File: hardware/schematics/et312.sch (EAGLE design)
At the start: 119 parts, among them IC1 LM324N, IC2 4066N, IC3 LM358, IC4 7809, IC5 LM358N, IC6 7809, J1 BATTERY_CONNDEANS, Q1 IRL520N-H, Q2 IRL520N-H, Q3 IRF9Z24, Q4 IRL520N-H, Q5 IRL520N-H, Q6 IRF9Z24, Q7 2N3906, T1 2N3904, U1 MEGA16-P, U9 7805, X1 HD44780LCD-1602, X2 STEREOJACK, X3 STEREOJACK, X4 STEREOJACK, X5 STEREOJACK, X6 STEREOJACK

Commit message: Schematics
WIP
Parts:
- removed T2, T3: (no value), Eagle_POWER_MAGNETICS_rev16b:WE-FB_LT35XX/LT3748_EFD25_750310988
- added TR1, TR2: 42TL025, trafo-xicon:42TL025
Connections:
- removed net N$66: T3.3, X6.1
- removed net N$67: T3.2, X6.2, X6.5
- removed net N$77: T2.3, X5.1
- removed net N$78: T2.2, X5.2, X5.5
- new net N$16: TR1.6, X5.2, X5.5
- new net N$49: TR2.6, X6.2, X6.5
- new net N$50: TR2.4, X6.1
- new net N$6: TR1.4, X5.1
- net N$34: now also TR1.1; no longer T2.1
- net N$35: now also TR1.2; no longer T2.5
- net N$36: now also TR2.1; no longer T3.1
- net N$37: now also TR2.2; no longer T3.5
- net N$38: now also TR2.3; no longer T3.4
- net N$39: now also TR1.3; no longer T2.4
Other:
- note removed: "Possible transformer: Wurth 750811048"
- moved on the sheet: X5, X6
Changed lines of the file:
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@@
 <part name="R52" library="eagle-ltspice" deviceset="R" device="0207/10" value="0.5R"/>
 <part name="GND21" library="supply1" deviceset="GND" device=""/>
-<part name="T2" library="Eagle_POWER_MAGNETICS_rev16b" deviceset="WE-FB_LT35XX/LT3748_EFD25_750310988" device=""/>
-<part name="T3" library="Eagle_POWER_MAGNETICS_rev16b" deviceset="WE-FB_LT35XX/LT3748_EFD25_750310988" device=""/>
+<part name="TR1" library="trafo-xicon" deviceset="42T?*" device="L" technology="025"/>
+<part name="TR2" library="trafo-xicon" deviceset="42T?*" device="L" technology="025"/>
 </parts>
 <sheets>
@@
 <plain>
 <text x="99.06" y="7.62" size="1.778" layer="91">Output Stage</text>
-<text x="157.48" y="119.38" size="1.27" layer="97">Possible transformer: Wurth 750811048</text>
 </plain>
 <instances>
@@
 <instance part="+9V5" gate="G$1" x="60.96" y="142.24"/>
 <instance part="+9V6" gate="G$1" x="109.22" y="111.76"/>
-<instance part="X5" gate="1" x="187.96" y="134.62"/>
-<instance part="X6" gate="1" x="187.96" y="53.34"/>
+<instance part="X5" gate="1" x="195.58" y="134.62"/>
+<instance part="X6" gate="1" x="195.58" y="53.34"/>
 <instance part="R52" gate="G$1" x="40.64" y="154.94" rot="R90"/>
 <instance part="GND21" gate="1" x="40.64" y="144.78"/>
-<instance part="T2" gate="G$1" x="162.56" y="132.08"/>
-<instance part="T3" gate="G$1" x="162.56" y="50.8"/>
+<instance part="TR1" gate="G$1" x="167.64" y="132.08"/>
+<instance part="TR2" gate="G$1" x="167.64" y="50.8"/>
 </instances>
 <busses>
@@
 <wire x1="121.92" y1="157.48" x2="152.4" y2="157.48" width="0.1524" layer="91"/>
 <wire x1="152.4" y1="157.48" x2="152.4" y2="137.16" width="0.1524" layer="91"/>
-<wire x1="157.48" y1="137.16" x2="152.4" y2="137.16" width="0.1524" layer="91"/>
-<pinref part="T2" gate="G$1" pin="1"/>
+<wire x1="160.02" y1="137.16" x2="152.4" y2="137.16" width="0.1524" layer="91"/>
+<pinref part="TR1" gate="G$1" pin="1"/>
 </segment>
 </net>
@@
 <segment>
 <pinref part="Q3" gate="G$1" pin="D"/>
-<wire x1="124.46" y1="132.08" x2="157.48" y2="132.08" width="0.1524" layer="91"/>
-<pinref part="T2" gate="G$1" pin="5"/>
+<wire x1="124.46" y1="132.08" x2="160.02" y2="132.08" width="0.1524" layer="91"/>
+<pinref part="TR1" gate="G$1" pin="2"/>
 </segment>
 </net>
@@
 <wire x1="121.92" y1="81.28" x2="152.4" y2="81.28" width="0.1524" layer="91"/>
 <wire x1="152.4" y1="81.28" x2="152.4" y2="55.88" width="0.1524" layer="91"/>
-<wire x1="157.48" y1="55.88" x2="152.4" y2="55.88" width="0.1524" layer="91"/>
-<pinref part="T3" gate="G$1" pin="1"/>
+<wire x1="160.02" y1="55.88" x2="152.4" y2="55.88" width="0.1524" layer="91"/>
+<pinref part="TR2" gate="G$1" pin="1"/>
 </segment>
 </net>
@@
 <segment>
 <pinref part="Q6" gate="G$1" pin="D"/>
-<wire x1="124.46" y1="50.8" x2="157.48" y2="50.8" width="0.1524" layer="91"/>
-<pinref part="T3" gate="G$1" pin="5"/>
+<wire x1="124.46" y1="50.8" x2="160.02" y2="50.8" width="0.1524" layer="91"/>
+<pinref part="TR2" gate="G$1" pin="2"/>
 </segment>
 </net>
@@
 <wire x1="124.46" y1="22.86" x2="152.4" y2="22.86" width="0.1524" layer="91"/>
 <wire x1="152.4" y1="22.86" x2="152.4" y2="45.72" width="0.1524" layer="91"/>
-<wire x1="157.48" y1="45.72" x2="152.4" y2="45.72" width="0.1524" layer="91"/>
-<pinref part="T3" gate="G$1" pin="4"/>
+<wire x1="160.02" y1="45.72" x2="152.4" y2="45.72" width="0.1524" layer="91"/>
+<pinref part="TR2" gate="G$1" pin="3"/>
 </segment>
 </net>
@@
 <wire x1="124.46" y1="104.14" x2="152.4" y2="104.14" width="0.1524" layer="91"/>
 <wire x1="152.4" y1="104.14" x2="152.4" y2="127" width="0.1524" layer="91"/>
-<wire x1="157.48" y1="127" x2="152.4" y2="127" width="0.1524" layer="91"/>
-<pinref part="T2" gate="G$1" pin="4"/>
+<wire x1="160.02" y1="127" x2="152.4" y2="127" width="0.1524" layer="91"/>
+<pinref part="TR1" gate="G$1" pin="3"/>
 </segment>
 </net>
@@
 </segment>
 </net>
-<net name="N$66" class="0">
-<segment>
-<pinref part="X6" gate="1" pin="1"/>
-<wire x1="175.26" y1="45.72" x2="170.18" y2="45.72" width="0.1524" layer="91"/>
-<wire x1="170.18" y1="45.72" x2="170.18" y2="48.26" width="0.1524" layer="91"/>
-<wire x1="170.18" y1="48.26" x2="167.64" y2="48.26" width="0.1524" layer="91"/>
-<pinref part="T3" gate="G$1" pin="3"/>
-</segment>
-</net>
-<net name="N$67" class="0">
-<segment>
-<pinref part="X6" gate="1" pin="5"/>
-<wire x1="175.26" y1="55.88" x2="172.72" y2="55.88" width="0.1524" layer="91"/>
-<pinref part="X6" gate="1" pin="2"/>
-<wire x1="172.72" y1="55.88" x2="172.72" y2="53.34" width="0.1524" layer="91"/>
-<wire x1="172.72" y1="53.34" x2="172.72" y2="48.26" width="0.1524" layer="91"/>
-<wire x1="172.72" y1="48.26" x2="175.26" y2="48.26" width="0.1524" layer="91"/>
-<pinref part="T3" gate="G$1" pin="2"/>
-<wire x1="167.64" y1="53.34" x2="172.72" y2="53.34" width="0.1524" layer="91"/>
-<junction x="172.72" y="53.34"/>
-</segment>
-</net>
-<net name="N$77" class="0">
-<segment>
-<pinref part="X5" gate="1" pin="1"/>
-<wire x1="175.26" y1="127" x2="170.18" y2="127" width="0.1524" layer="91"/>
-<wire x1="170.18" y1="127" x2="170.18" y2="129.54" width="0.1524" layer="91"/>
-<wire x1="170.18" y1="129.54" x2="167.64" y2="129.54" width="0.1524" layer="91"/>
-<pinref part="T2" gate="G$1" pin="3"/>
-</segment>
-</net>
-<net name="N$78" class="0">
-<segment>
-<pinref part="X5" gate="1" pin="5"/>
-<wire x1="175.26" y1="137.16" x2="172.72" y2="137.16" width="0.1524" layer="91"/>
-<pinref part="X5" gate="1" pin="2"/>
-<wire x1="172.72" y1="137.16" x2="172.72" y2="134.62" width="0.1524" layer="91"/>
-<wire x1="172.72" y1="134.62" x2="172.72" y2="129.54" width="0.1524" layer="91"/>
-<wire x1="172.72" y1="129.54" x2="175.26" y2="129.54" width="0.1524" layer="91"/>
-<pinref part="T2" gate="G$1" pin="2"/>
-<wire x1="167.64" y1="134.62" x2="172.72" y2="134.62" width="0.1524" layer="91"/>
-<junction x="172.72" y="134.62"/>
-</segment>
-</net>
 <net name="PB2" class="0">
 <segment>
@@
 </segment>
 </net>
+<net name="N$6" class="0">
+<segment>
+<pinref part="TR1" gate="G$1" pin="4"/>
+<pinref part="X5" gate="1" pin="1"/>
+<wire x1="177.8" y1="127" x2="182.88" y2="127" width="0.1524" layer="91"/>
+</segment>
+</net>
+<net name="N$16" class="0">
+<segment>
+<pinref part="TR1" gate="G$1" pin="6"/>
+<pinref part="X5" gate="1" pin="5"/>
+<wire x1="177.8" y1="137.16" x2="180.34" y2="137.16" width="0.1524" layer="91"/>
+<pinref part="X5" gate="1" pin="2"/>
+<wire x1="180.34" y1="137.16" x2="182.88" y2="137.16" width="0.1524" layer="91"/>
+<wire x1="182.88" y1="129.54" x2="180.34" y2="129.54" width="0.1524" layer="91"/>
+<wire x1="180.34" y1="129.54" x2="180.34" y2="137.16" width="0.1524" layer="91"/>
+<junction x="180.34" y="137.16"/>
+</segment>
+</net>
+<net name="N$49" class="0">
+<segment>
+<pinref part="TR2" gate="G$1" pin="6"/>
+<pinref part="X6" gate="1" pin="5"/>
+<wire x1="177.8" y1="55.88" x2="180.34" y2="55.88" width="0.1524" layer="91"/>
+<wire x1="180.34" y1="55.88" x2="182.88" y2="55.88" width="0.1524" layer="91"/>
+<wire x1="180.34" y1="55.88" x2="180.34" y2="48.26" width="0.1524" layer="91"/>
+<pinref part="X6" gate="1" pin="2"/>
+<wire x1="180.34" y1="48.26" x2="182.88" y2="48.26" width="0.1524" layer="91"/>
+<junction x="180.34" y="55.88"/>
+</segment>
+</net>
+<net name="N$50" class="0">
+<segment>
+<pinref part="TR2" gate="G$1" pin="4"/>
+<pinref part="X6" gate="1" pin="1"/>
+<wire x1="177.8" y1="45.72" x2="182.88" y2="45.72" width="0.1524" layer="91"/>
+</segment>
+</net>

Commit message: Arduino Sheild Eagle
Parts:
- R23, R24: device rcl:R-EU_0207/10 -> rcl:R-EU_0204/7
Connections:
- net +12V: no longer C7.+, L1.2
- net N$31: now also C7.+, L1.2; no longer L1.1
- net V+: now also L1.1
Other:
- moved on the sheet: C5, C7, J1, JP1, L1

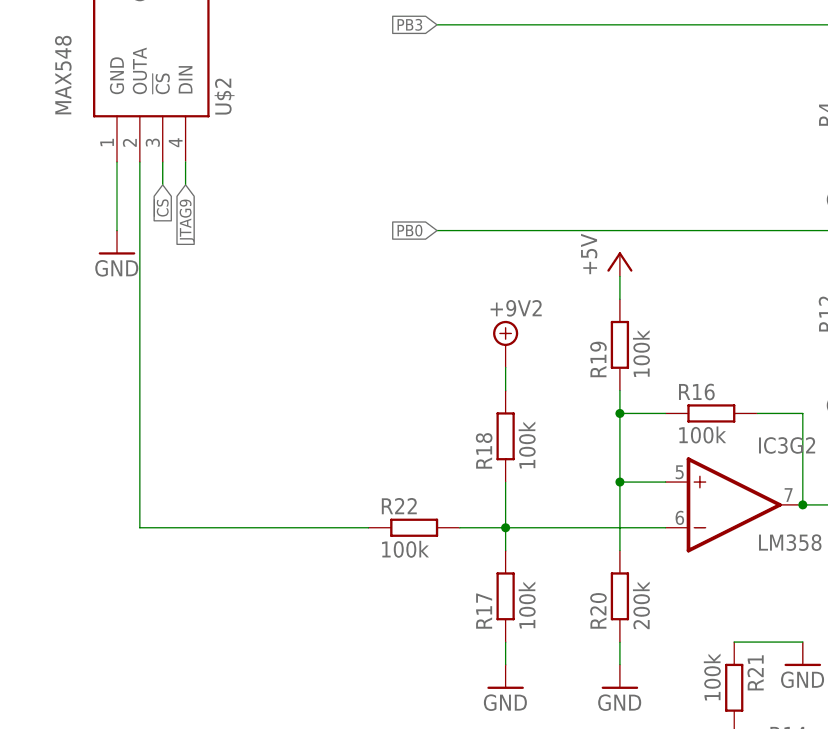
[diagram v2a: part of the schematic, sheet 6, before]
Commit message: Pin Swap
et312.sch page 6 vs 03_output_stage_1.gif, bottom opamp (pins 5 & 6)
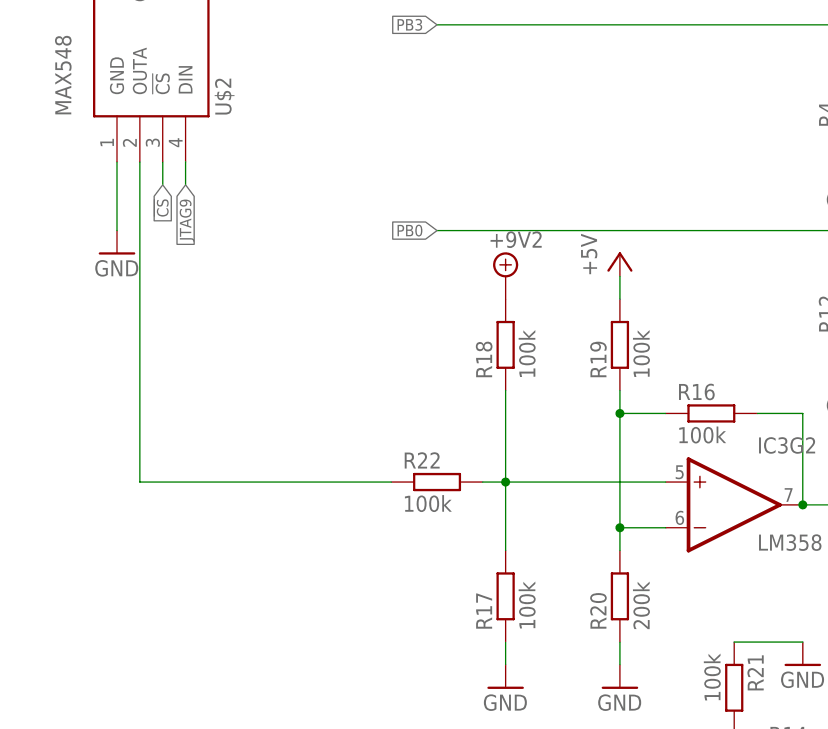
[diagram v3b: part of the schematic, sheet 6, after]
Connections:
- net N$28: now also IC3G2.+IN; no longer IC3G2.-IN
- net N$41: now also IC3G2.-IN; no longer IC3G2.+IN
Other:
- moved on the sheet: R18, R22
